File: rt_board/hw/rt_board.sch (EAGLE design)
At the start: 67 parts, among them IC1 MCP170333MB, IC2/L1 TLE4935L, IC3/L1 TLE4935L, IC4/L1 TLE4935L, IC5/L1 TLE4935L, Q1 8MHz, SW1 B3U-1000PM-B, SW2 B3U-1000PM-B, U1 DRV8801PWP, U2 DRV8801PWP, U3 SN74AVC4T245PW, U4 ACS712ELCTR-05B-T, U5 ACS712ELCTR-05B-T, U6 STM32F051R8T7, X1 LEFT, X2 RIGHT, X3 PWR

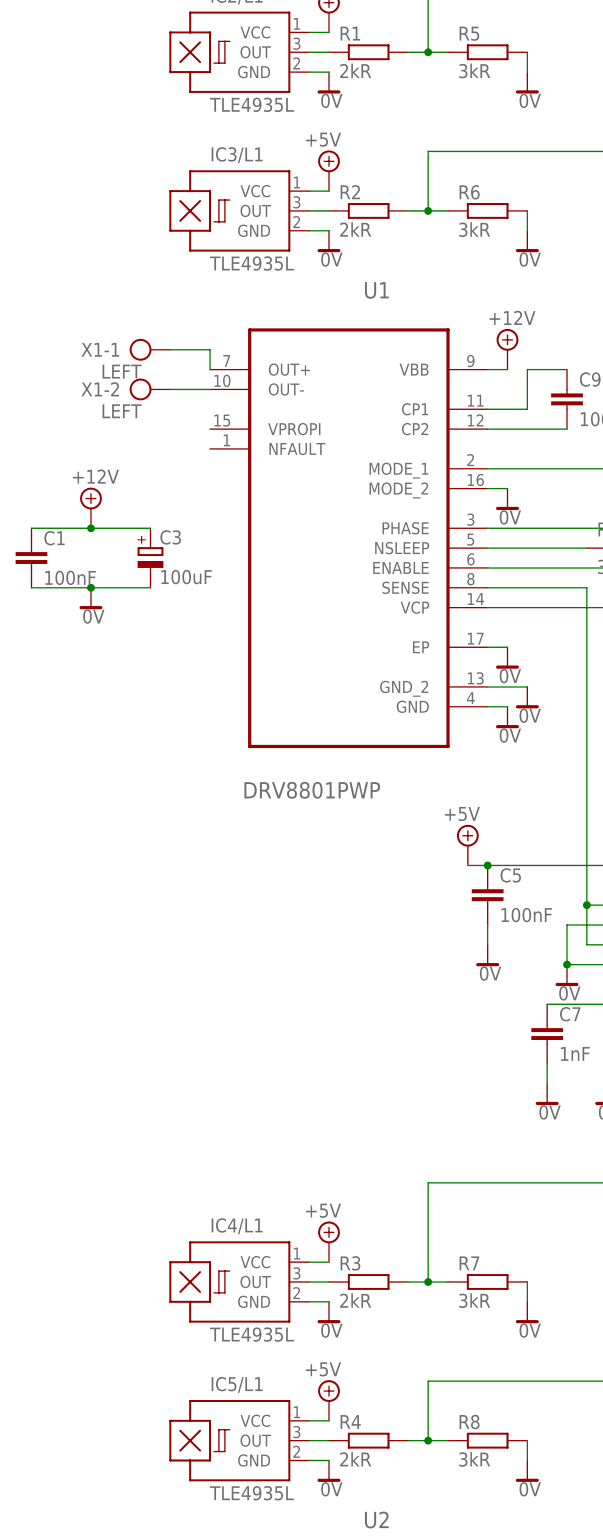
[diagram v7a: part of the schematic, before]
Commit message: fixed layout of names and values of devices, so that it is readable
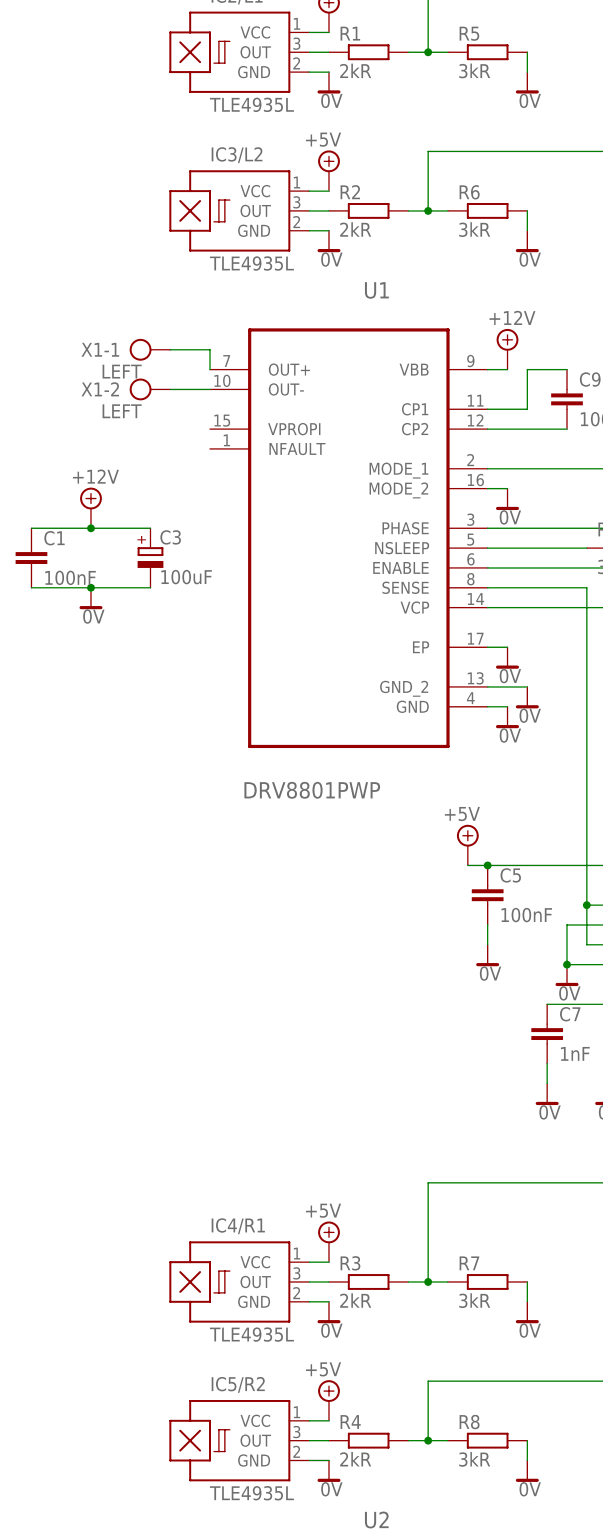
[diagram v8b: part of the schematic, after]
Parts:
- renumbered IC3/L1 to IC3/L2, IC4/L1 to IC4/R1, IC5/L1 to IC5/R2
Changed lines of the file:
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@@
 <part name="R5" library="rcl" deviceset="R-EU_" device="R0603" value="3kR"/>
 <part name="SUPPLY41" library="supply2" deviceset="0V" device=""/>
-<part name="IC3/L1" library="allegro" deviceset="A12*?" device="UA" technology="02" value="TLE4935L"/>
+<part name="IC3/L2" library="allegro" deviceset="A12*?" device="UA" technology="02" value="TLE4935L"/>
 <part name="SUPPLY42" library="supply2" deviceset="0V" device=""/>
 <part name="SUPPLY43" library="supply2" deviceset="+5V/1" device="" value="+5V"/>
@@
 <part name="C9" library="rcl" deviceset="C-EU" device="C1206" value="100nF"/>
 <part name="SUPPLY58" library="supply2" deviceset="0V" device=""/>
-<part name="IC4/L1" library="allegro" deviceset="A12*?" device="UA" technology="02" value="TLE4935L"/>
+<part name="IC4/R1" library="allegro" deviceset="A12*?" device="UA" technology="02" value="TLE4935L"/>
 <part name="SUPPLY60" library="supply2" deviceset="0V" device=""/>
 <part name="SUPPLY61" library="supply2" deviceset="+5V/1" device="" value="+5V"/>
@@
 <part name="R7" library="rcl" deviceset="R-EU_" device="R0603" value="3kR"/>
 <part name="SUPPLY62" library="supply2" deviceset="0V" device=""/>
-<part name="IC5/L1" library="allegro" deviceset="A12*?" device="UA" technology="02" value="TLE4935L"/>
+<part name="IC5/R2" library="allegro" deviceset="A12*?" device="UA" technology="02" value="TLE4935L"/>
 <part name="SUPPLY63" library="supply2" deviceset="0V" device=""/>
 <part name="SUPPLY64" library="supply2" deviceset="+5V/1" device="" value="+5V"/>
@@
 <instance part="R5" gate="G$1" x="-180.34" y="20.32"/>
 <instance part="SUPPLY41" gate="0V" x="-175.26" y="15.24"/>
-<instance part="IC3/L1" gate="G$1" x="-210.82" y="0"/>
+<instance part="IC3/L2" gate="G$1" x="-210.82" y="0"/>
 <instance part="SUPPLY42" gate="0V" x="-200.66" y="-5.08"/>
 <instance part="SUPPLY43" gate="G$1" x="-200.66" y="5.08"/>
@@
 <instance part="C9" gate="G$1" x="-170.18" y="-22.86"/>
 <instance part="SUPPLY58" gate="0V" x="-177.8" y="-58.42"/>
-<instance part="IC4/L1" gate="G$1" x="-210.82" y="-137.16"/>
+<instance part="IC4/R1" gate="G$1" x="-210.82" y="-137.16"/>
 <instance part="SUPPLY60" gate="0V" x="-200.66" y="-142.24"/>
 <instance part="SUPPLY61" gate="G$1" x="-200.66" y="-132.08"/>
@@
 <instance part="R7" gate="G$1" x="-180.34" y="-137.16"/>
 <instance part="SUPPLY62" gate="0V" x="-175.26" y="-142.24"/>
-<instance part="IC5/L1" gate="G$1" x="-210.82" y="-157.48"/>
+<instance part="IC5/R2" gate="G$1" x="-210.82" y="-157.48"/>
 <instance part="SUPPLY63" gate="0V" x="-200.66" y="-162.56"/>
 <instance part="SUPPLY64" gate="G$1" x="-200.66" y="-152.4"/>
@@
 </segment>
 <segment>
-<pinref part="IC3/L1" gate="G$1" pin="GND"/>
+<pinref part="IC3/L2" gate="G$1" pin="GND"/>
 <pinref part="SUPPLY42" gate="0V" pin="0V"/>
 <wire x1="-203.2" y1="-2.54" x2="-200.66" y2="-2.54" width="0.1524" layer="91"/>
@@
 </segment>
 <segment>
-<pinref part="IC4/L1" gate="G$1" pin="GND"/>
+<pinref part="IC4/R1" gate="G$1" pin="GND"/>
 <pinref part="SUPPLY60" gate="0V" pin="0V"/>
 <wire x1="-203.2" y1="-139.7" x2="-200.66" y2="-139.7" width="0.1524" layer="91"/>
@@
 </segment>
 <segment>
-<pinref part="IC5/L1" gate="G$1" pin="GND"/>
+<pinref part="IC5/R2" gate="G$1" pin="GND"/>
 <pinref part="SUPPLY63" gate="0V" pin="0V"/>
 <wire x1="-203.2" y1="-160.02" x2="-200.66" y2="-160.02" width="0.1524" layer="91"/>
@@
 </segment>
 <segment>
-<pinref part="IC3/L1" gate="G$1" pin="VCC"/>
+<pinref part="IC3/L2" gate="G$1" pin="VCC"/>
 <pinref part="SUPPLY43" gate="G$1" pin="+5V/1"/>
 <wire x1="-200.66" y1="2.54" x2="-203.2" y2="2.54" width="0.1524" layer="91"/>
@@
 </segment>
 <segment>
-<pinref part="IC4/L1" gate="G$1" pin="VCC"/>
+<pinref part="IC4/R1" gate="G$1" pin="VCC"/>
 <pinref part="SUPPLY61" gate="G$1" pin="+5V/1"/>
 <wire x1="-200.66" y1="-134.62" x2="-203.2" y2="-134.62" width="0.1524" layer="91"/>
 </segment>
 <segment>
-<pinref part="IC5/L1" gate="G$1" pin="VCC"/>
+<pinref part="IC5/R2" gate="G$1" pin="VCC"/>
 <pinref part="SUPPLY64" gate="G$1" pin="+5V/1"/>
 <wire x1="-200.66" y1="-154.94" x2="-203.2" y2="-154.94" width="0.1524" layer="91"/>
@@
 <net name="N$18" class="0">
 <segment>
-<pinref part="IC3/L1" gate="G$1" pin="OUT"/>
+<pinref part="IC3/L2" gate="G$1" pin="OUT"/>
 <pinref part="R2" gate="G$1" pin="1"/>
 <wire x1="-200.66" y1="0" x2="-203.2" y2="0" width="0.1524" layer="91"/>
@@
 <net name="N$29" class="0">
 <segment>
-<pinref part="IC4/L1" gate="G$1" pin="OUT"/>
+<pinref part="IC4/R1" gate="G$1" pin="OUT"/>
 <pinref part="R3" gate="G$1" pin="1"/>
 <wire x1="-200.66" y1="-137.16" x2="-203.2" y2="-137.16" width="0.1524" layer="91"/>
@@
 <net name="N$31" class="0">
 <segment>
-<pinref part="IC5/L1" gate="G$1" pin="OUT"/>
+<pinref part="IC5/R2" gate="G$1" pin="OUT"/>
 <pinref part="R4" gate="G$1" pin="1"/>
 <wire x1="-200.66" y1="-157.48" x2="-203.2" y2="-157.48" width="0.1524" layer="91"/>
